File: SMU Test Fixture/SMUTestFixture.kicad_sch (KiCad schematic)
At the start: 43 parts

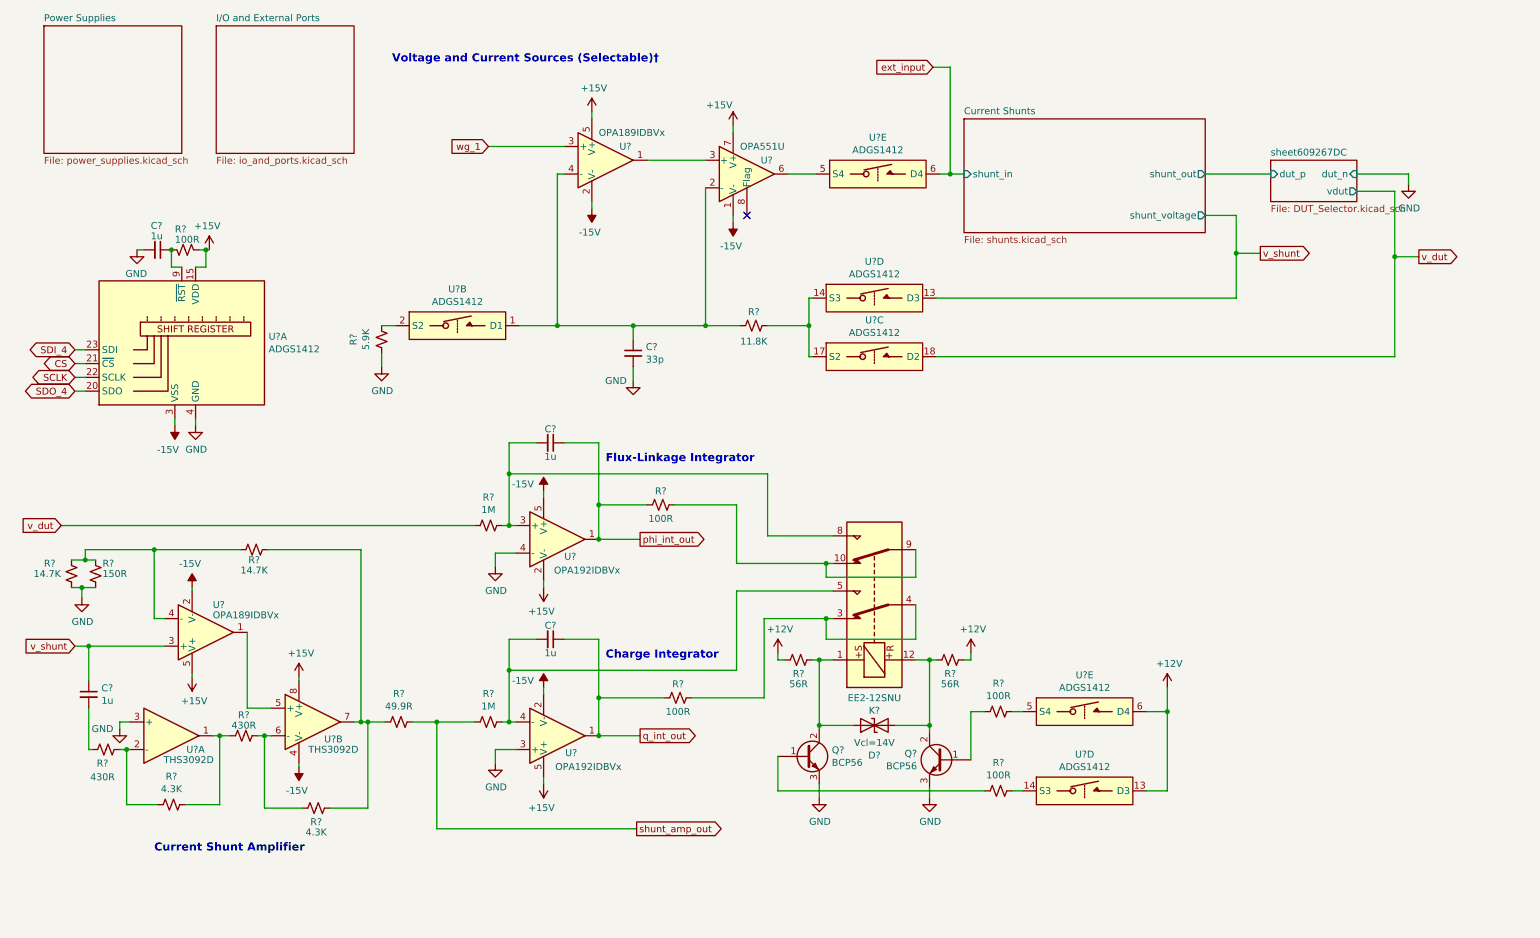
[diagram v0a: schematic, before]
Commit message: Move bypass caps to devices
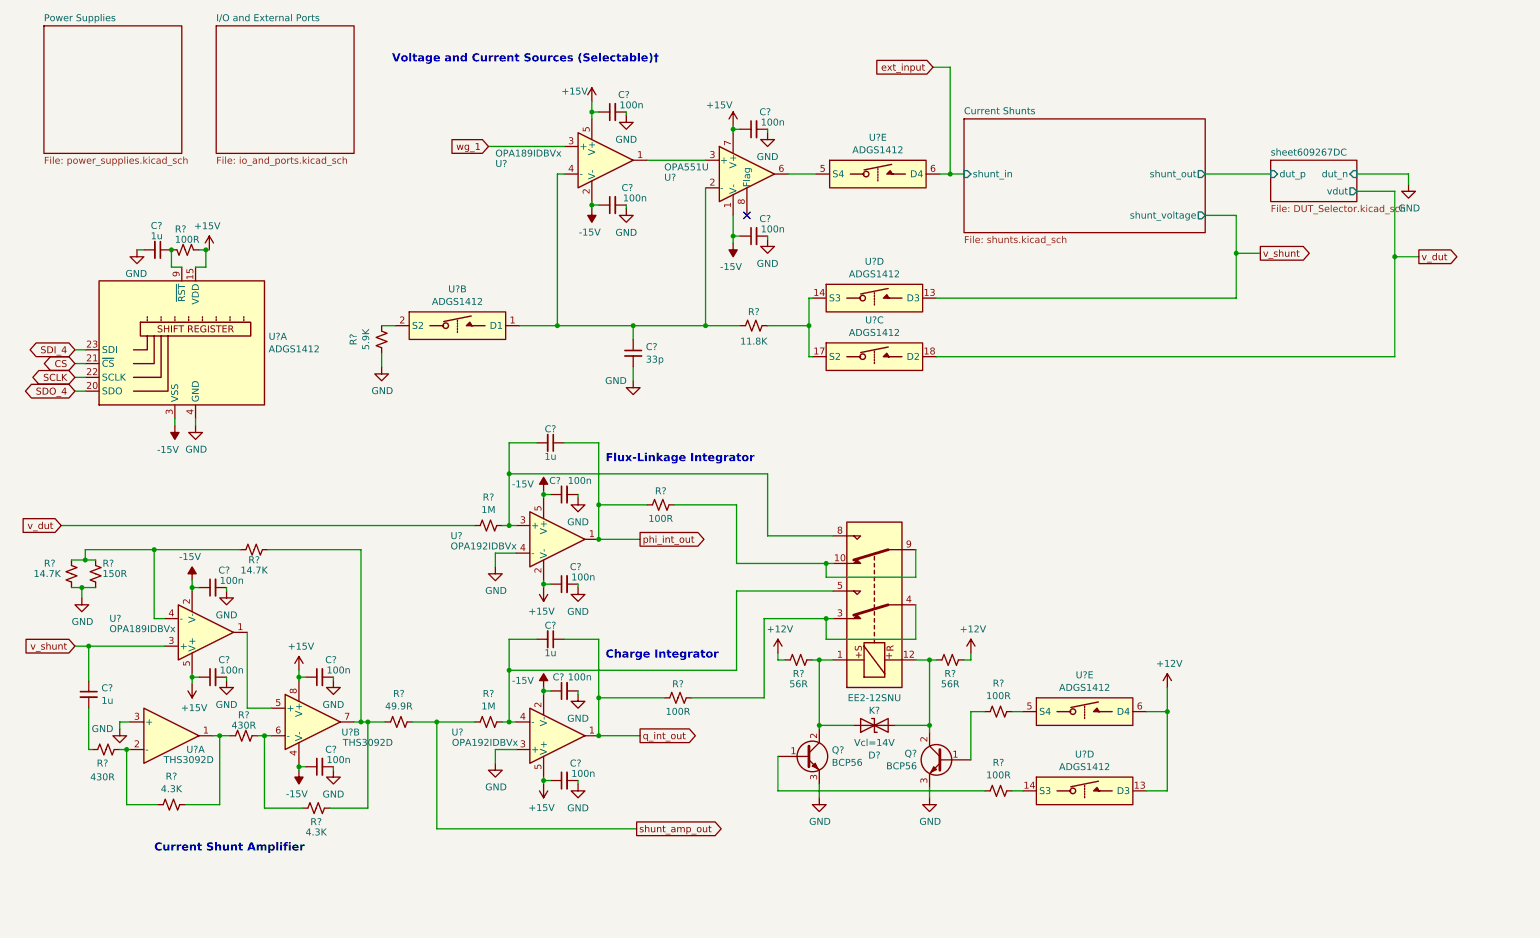
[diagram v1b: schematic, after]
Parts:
- added C? (x12): 100n, Capacitor_SMD:C_0805_2012Metric_Pad1.18x1.45mm_HandSolder, symbol Device:C_Small
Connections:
- net +15V: now also C?.1, C?.1, C?.1, C?.1, C?.1, C?.1
- net -15V: now also C?.1, C?.1, C?.1, C?.1, C?.1, C?.1
- net GND: now also C?.2, C?.2, C?.2, C?.2, C?.2, C?.2, C?.2, C?.2, C?.2, C?.2, C?.2, C?.2

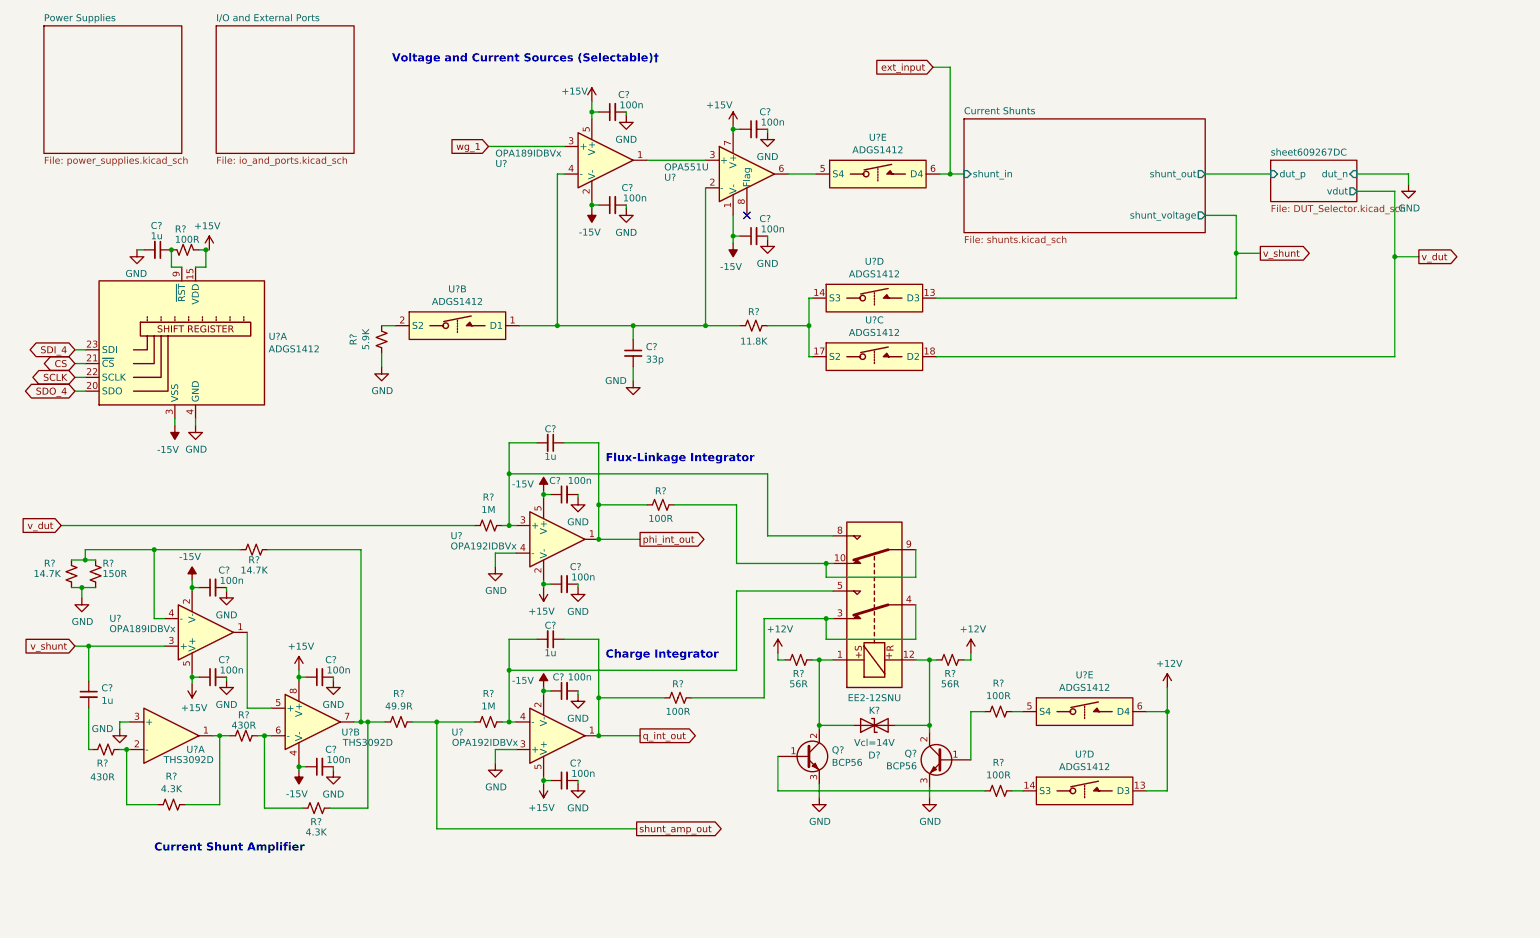
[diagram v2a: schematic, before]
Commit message: Add buffered vdut output
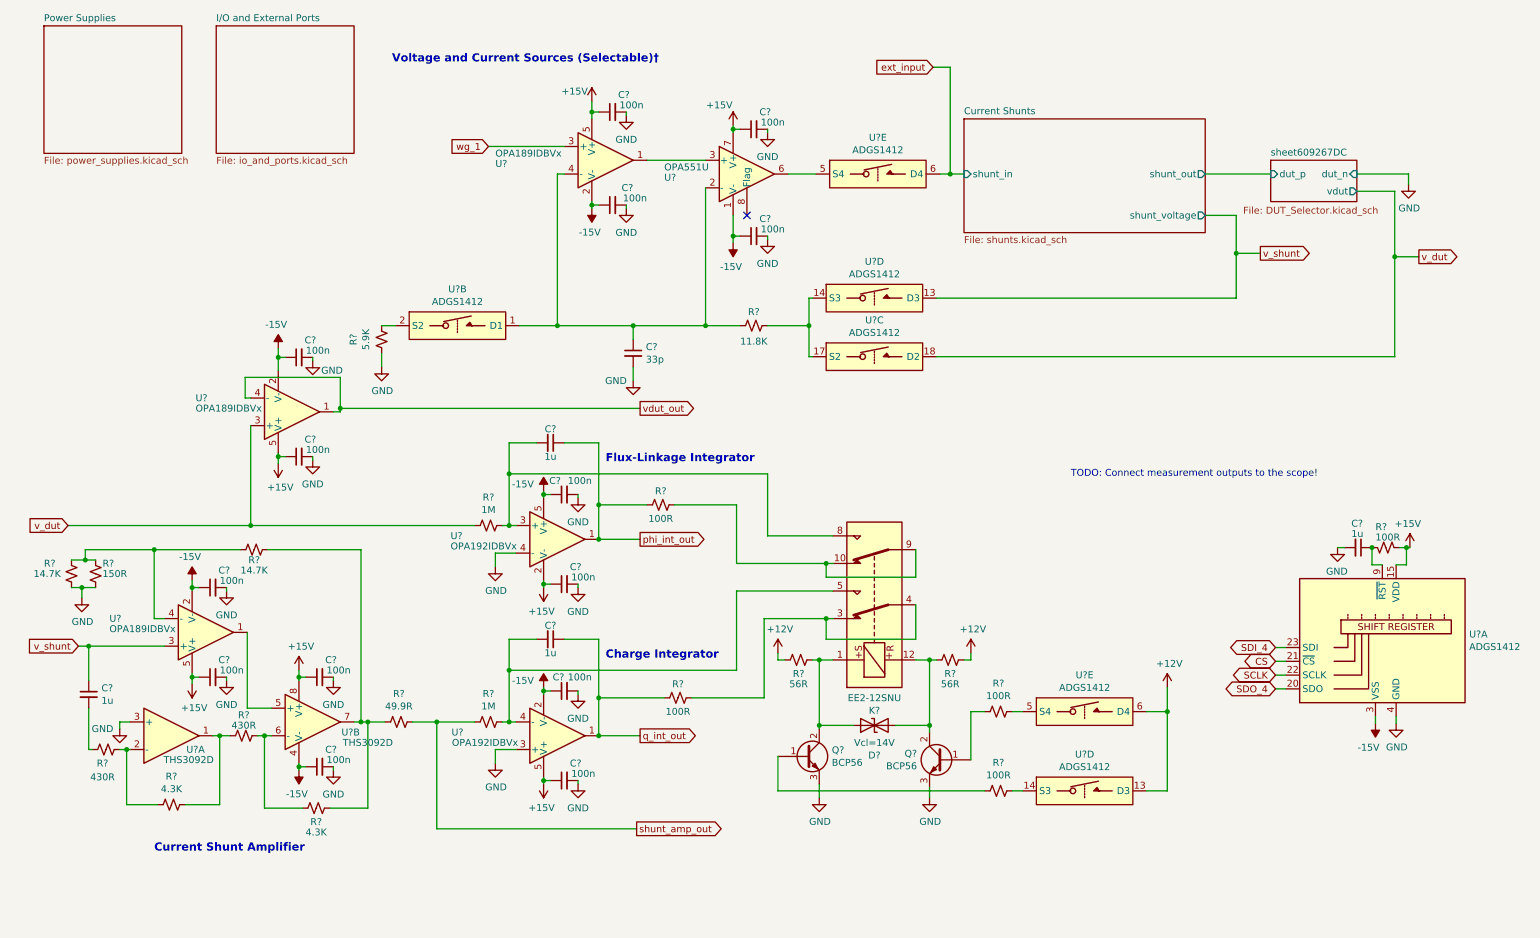
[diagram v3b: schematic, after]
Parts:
- added C? (x2): 100n, Capacitor_SMD:C_0805_2012Metric_Pad1.18x1.45mm_HandSolder, symbol Device:C_Small
- added U?: OPA189IDBVx, Package_TO_SOT_SMD:SOT-23-5_HandSoldering, symbol SMUTestFixture-rescue:OPA189IDBVx-MAGI_Symbols
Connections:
- net +15V: now also C?.1, U?.5 (V+)
- net -15V: now also C?.1, U?.2 (V-)
- net GND: now also C?.2, C?.2
- net v_dut: now also U?.3 (+)
- new net vdut_out: U?.1, U?.4 (-)
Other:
- note added: "TODO: Connect measurement outputs to the scope!"
- moved on the sheet: C?, R?, U?A

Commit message: Add measurement connections to scope inputs
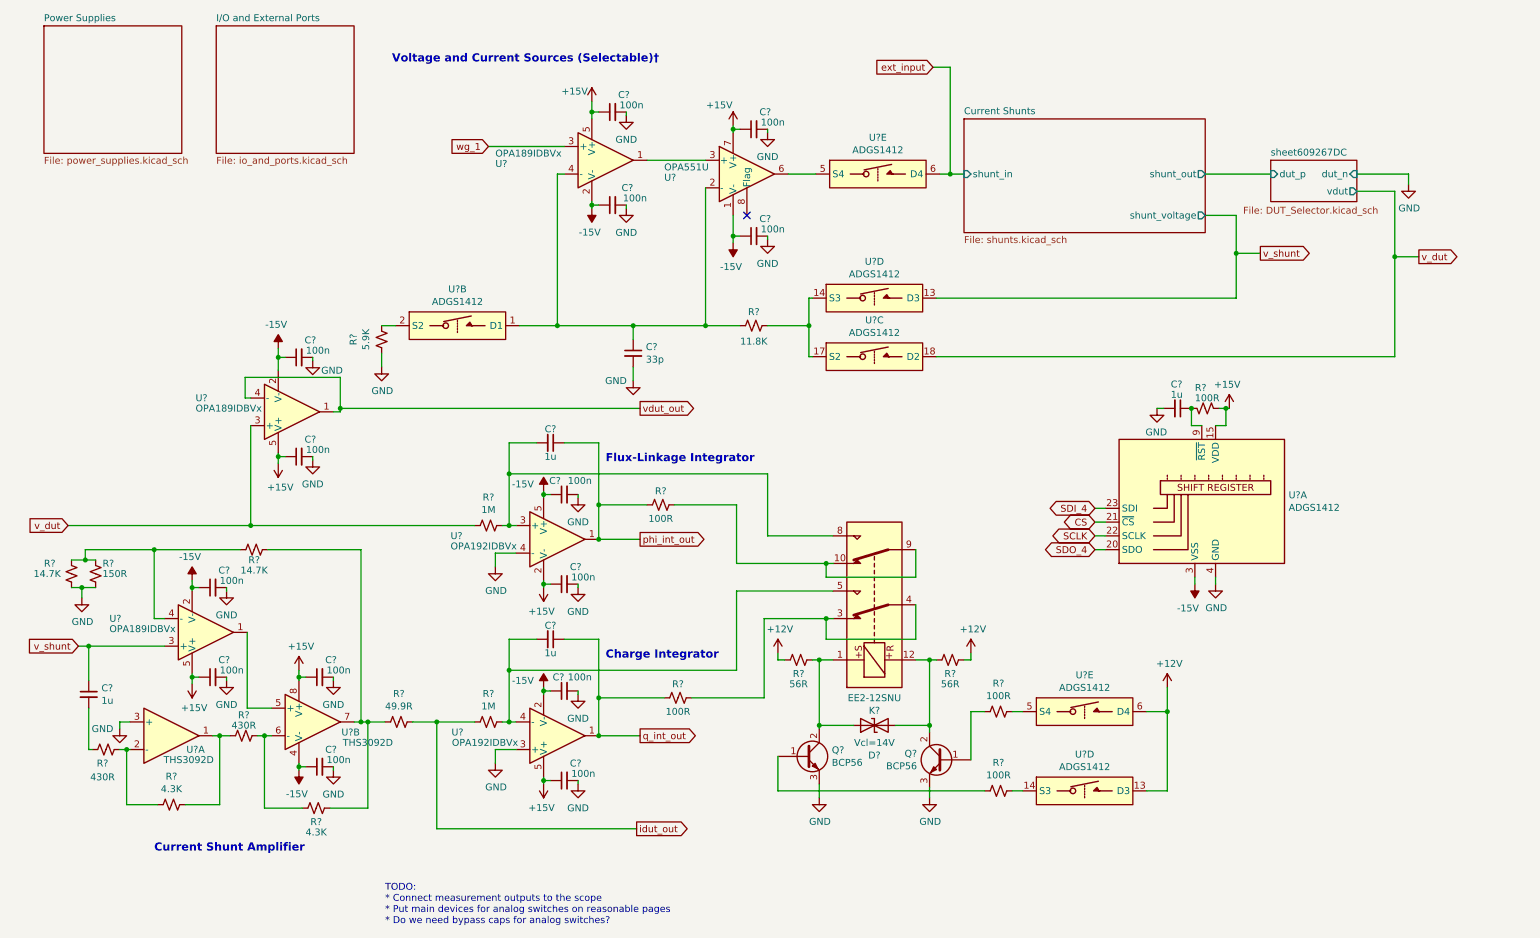
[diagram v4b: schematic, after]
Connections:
- net shunt_amp_out renamed idut_out
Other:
- note added: "TODO: * Connect measurement outputs to the scope * Put main devices for analog switches on reasonable pages * Do we need bypass caps for analog switches?"
- note removed: "TODO: Connect measurement outputs to the scope!"
- moved on the sheet: C?, R?, U?A

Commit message: Fix grid nightmare. Begin adding bypass caps for a.switches
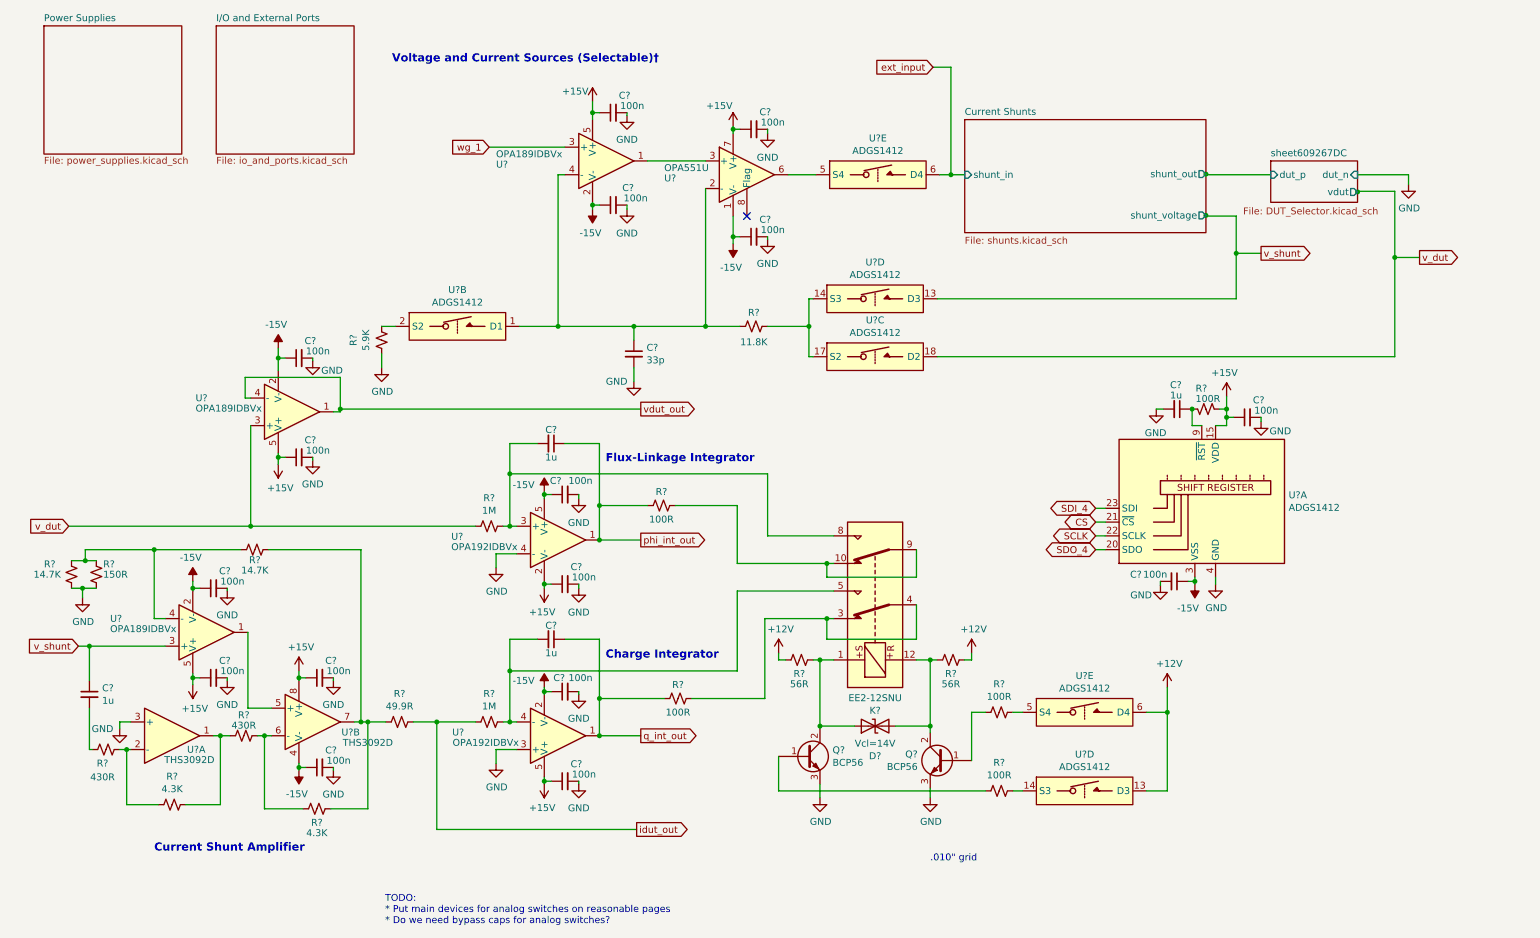
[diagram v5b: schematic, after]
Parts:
- added C? (x2): 100n, Capacitor_SMD:C_0805_2012Metric_Pad1.18x1.45mm_HandSolder, symbol Device:C_Small
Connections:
- net +15V: now also C?.1
- net -15V: now also C?.1
- net GND: now also C?.2, C?.2
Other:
- note added: ".010" grid"
- note added: "TODO: * Put main devices for analog switches on reasonable pages * Do we need bypass caps for analog switches?"
- note removed: "TODO: * Connect measurement outputs to the scope * Put main devices for analog switches on reasonable pages * Do we need bypass caps for analog switches?"

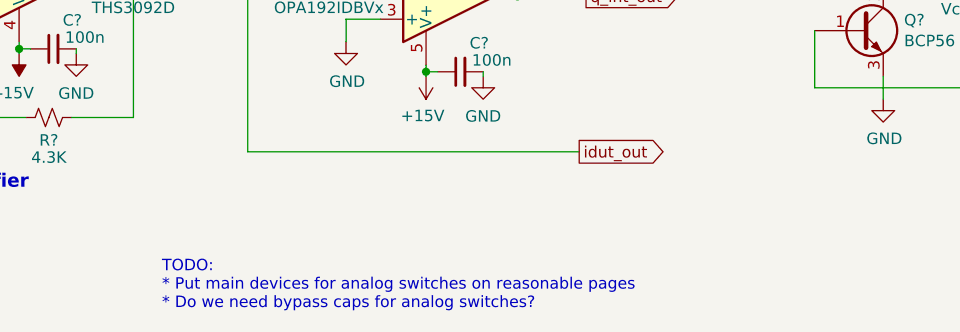
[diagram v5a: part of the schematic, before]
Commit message: Finish adding bypass for all a.switches
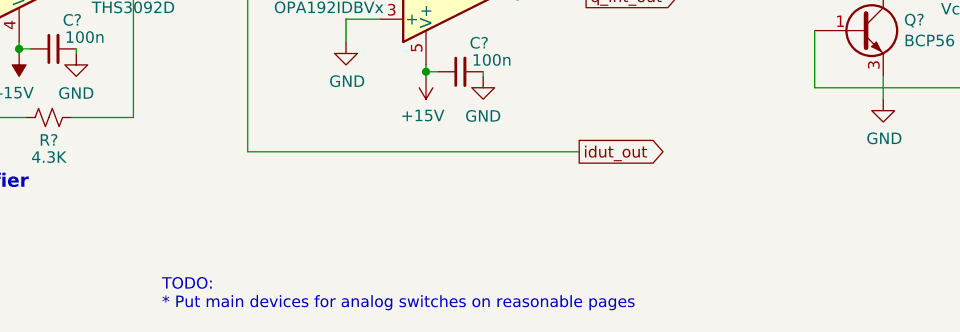
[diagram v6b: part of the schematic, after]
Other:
- note added: "TODO: * Put main devices for analog switches on reasonable pages"
- note removed: "TODO: * Put main devices for analog switches on reasonable pages * Do we need bypass caps for analog switches?"
